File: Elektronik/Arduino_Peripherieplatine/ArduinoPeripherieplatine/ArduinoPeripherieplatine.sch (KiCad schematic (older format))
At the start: 31 parts

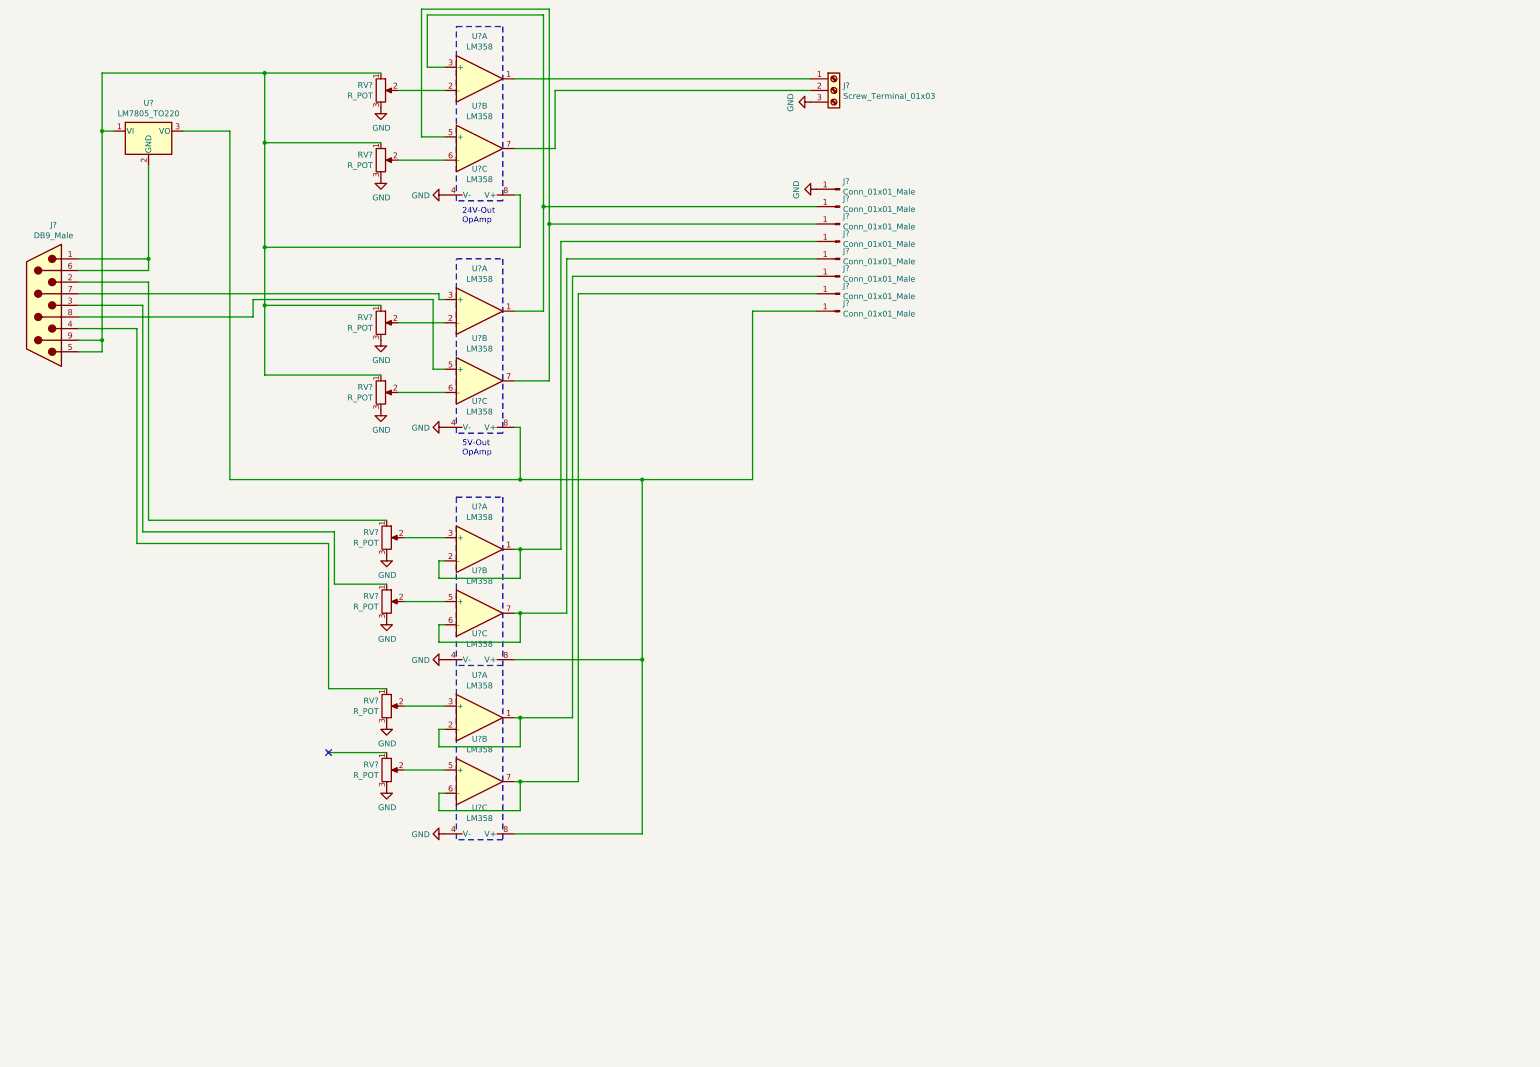
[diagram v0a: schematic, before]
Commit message: Updated Peripheral PCB
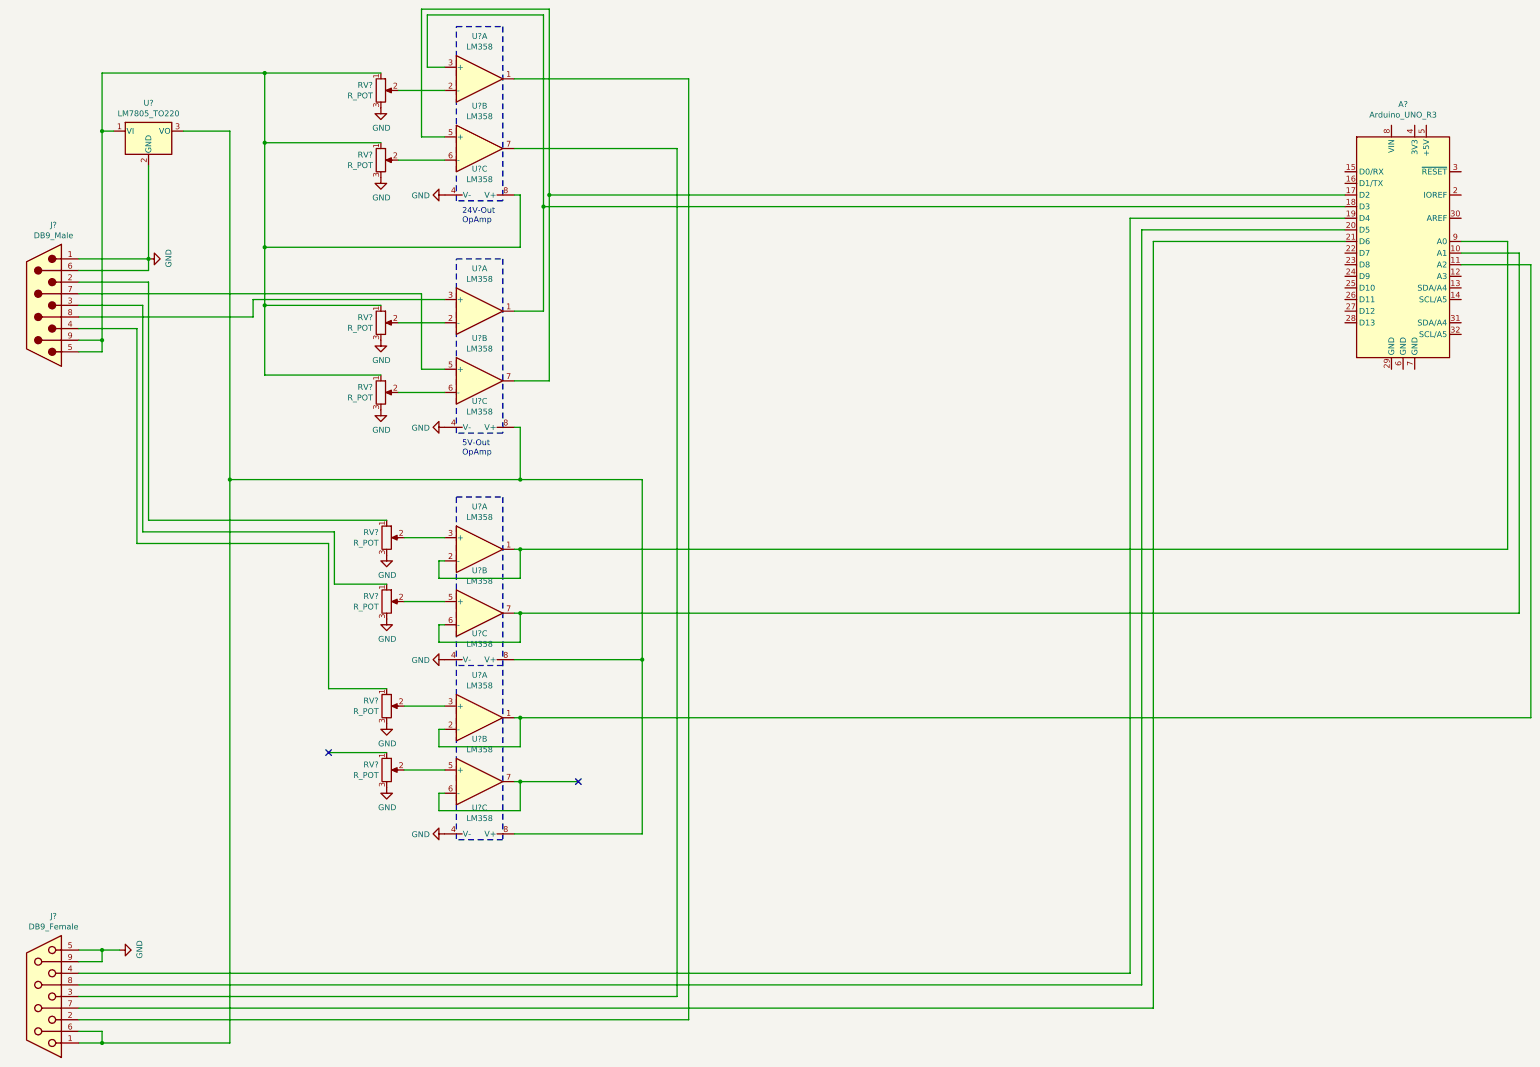
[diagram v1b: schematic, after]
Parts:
- removed J?: Screw_Terminal_01x03, symbol Connector:Screw_Terminal_01x03
- removed J? (x8): Conn_01x01_Male, symbol Connector:Conn_01x01_Male
- added A?: Arduino_UNO_R3, Module:Arduino_UNO_R3, symbol MCU_Module:Arduino_UNO_R3
- added J?: DB9_Female, symbol Connector:DB9_Female
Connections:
- net GND: now also J?.1, J?.6, U?.2 (GND), J?.5, J?.9
- net at U?.3 (VO), U?.8 (V+), U?.8 (V+)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: now also J?.1, J?.6
- net at U?.1: now also J?.2
- net at U?.1, U?.3 (+): now also A?.18 (D3)
- net at U?.5 (+), U?.7: now also A?.17 (D2)
- net at U?.7: now also J?.3
- net at U?.3 (+): now also J?.8; no longer J?.7
- net at U?.5 (+): now also J?.7; no longer J?.8
- net at U?.1, U?.2 (-): now also A?.9 (A0)
- net at U?.6 (-), U?.7: now also A?.10 (A1)
- net at U?.1, U?.2 (-): now also A?.11 (A2)
- new net: A?.19 (D4), J?.4
- new net: A?.21 (D6), J?.7
- new net: A?.20 (D5), J?.8
- no-connect marks 1 -> 2
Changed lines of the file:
@@
 EELAYER 30 0
 EELAYER END
-$Descr A4 11693 8268
+$Descr A3 16535 11693
 encoding utf-8
 Sheet 1 1
@@
 	4600 500  5700 500
 Wire Wire Line
-	5700 500  5700 2350
+	5700 500  5700 2100
 Wire Wire Line
 	5700 3700 5400 3700
@@
 Text Notes 4950 2350 0    50   ~ 0
 24V-Out\nOpAmp
-$Comp
-L Connector:Screw_Terminal_01x03 J?
-U 1 1 63429B53
-P 8150 1200
-F 0 "J?" H 8230 1242 50  0000 L CNN
-F 1 "Screw_Terminal_01x03" H 8230 1151 50  0000 L CNN
-F 2 "" H 8150 1200 50  0001 C CNN
-F 3 "~" H 8150 1200 50  0001 C CNN
-	1    8150 1200
-	1    0    0    -1
-$EndComp
-Wire Wire Line
-	5400 1100 7950 1100
-Wire Wire Line
-	5400 1700 5750 1700
-Wire Wire Line
-	5750 1700 5750 1200
-Wire Wire Line
-	5750 1200 7950 1200
-$Comp
-L power:GND #PWR?
-U 1 1 6342D1B7
-P 7950 1300
-F 0 "#PWR?" H 7950 1050 50  0001 C CNN
-F 1 "GND" H 7955 1127 50  0000 C CNN
-F 2 "" H 7950 1300 50  0001 C CNN
-F 3 "" H 7950 1300 50  0001 C CNN
-	1    7950 1300
-	0    1    1    0
-$EndComp
-$Comp
-L Connector:Conn_01x01_Male J?
-U 1 1 634336AF
-P 8200 2050
-F 0 "J?" H 8172 1982 50  0000 R CNN
-F 1 "Conn_01x01_Male" H 8172 2073 50  0000 R CNN
-F 2 "" H 8200 2050 50  0001 C CNN
-F 3 "~" H 8200 2050 50  0001 C CNN
-	1    8200 2050
-	-1   0    0    1
-$EndComp
-$Comp
-L Connector:Conn_01x01_Male J?
-U 1 1 63434368
-P 8200 2200
-F 0 "J?" H 8172 2132 50  0000 R CNN
-F 1 "Conn_01x01_Male" H 8172 2223 50  0000 R CNN
-F 2 "" H 8200 2200 50  0001 C CNN
-F 3 "~" H 8200 2200 50  0001 C CNN
-	1    8200 2200
-	-1   0    0    1
-$EndComp
-$Comp
-L Connector:Conn_01x01_Male J?
-U 1 1 634347F4
-P 8200 2350
-F 0 "J?" H 8172 2282 50  0000 R CNN
-F 1 "Conn_01x01_Male" H 8172 2373 50  0000 R CNN
-F 2 "" H 8200 2350 50  0001 C CNN
-F 3 "~" H 8200 2350 50  0001 C CNN
-	1    8200 2350
-	-1   0    0    1
-$EndComp
-$Comp
-L Connector:Conn_01x01_Male J?
-U 1 1 63434E46
-P 8200 2500
-F 0 "J?" H 8172 2432 50  0000 R CNN
-F 1 "Conn_01x01_Male" H 8172 2523 50  0000 R CNN
-F 2 "" H 8200 2500 50  0001 C CNN
-F 3 "~" H 8200 2500 50  0001 C CNN
-	1    8200 2500
-	-1   0    0    1
-$EndComp
-$Comp
-L Connector:Conn_01x01_Male J?
-U 1 1 63435092
-P 8200 2650
-F 0 "J?" H 8172 2582 50  0000 R CNN
-F 1 "Conn_01x01_Male" H 8172 2673 50  0000 R CNN
-F 2 "" H 8200 2650 50  0001 C CNN
-F 3 "~" H 8200 2650 50  0001 C CNN
-	1    8200 2650
-	-1   0    0    1
-$EndComp
-$Comp
-L Connector:Conn_01x01_Male J?
-U 1 1 63435409
-P 8200 2800
-F 0 "J?" H 8172 2732 50  0000 R CNN
-F 1 "Conn_01x01_Male" H 8172 2823 50  0000 R CNN
-F 2 "" H 8200 2800 50  0001 C CNN
-F 3 "~" H 8200 2800 50  0001 C CNN
-	1    8200 2800
-	-1   0    0    1
-$EndComp
-$Comp
-L Connector:Conn_01x01_Male J?
-U 1 1 634355C3
-P 8200 2950
-F 0 "J?" H 8172 2882 50  0000 R CNN
-F 1 "Conn_01x01_Male" H 8172 2973 50  0000 R CNN
-F 2 "" H 8200 2950 50  0001 C CNN
-F 3 "~" H 8200 2950 50  0001 C CNN
-	1    8200 2950
-	-1   0    0    1
-$EndComp
-$Comp
-L Connector:Conn_01x01_Male J?
-U 1 1 63435818
-P 8200 3100
-F 0 "J?" H 8172 3032 50  0000 R CNN
-F 1 "Conn_01x01_Male" H 8172 3123 50  0000 R CNN
-F 2 "" H 8200 3100 50  0001 C CNN
-F 3 "~" H 8200 3100 50  0001 C CNN
-	1    8200 3100
-	-1   0    0    1
-$EndComp
+Wire Wire Line
+	5400 1100 6900 1100
 Wire Wire Line
 	5450 4550 6500 4550
-Wire Wire Line
-	7450 4550 7450 3100
-Wire Wire Line
-	7450 3100 8000 3100
 Connection ~ 5450 4550
-$Comp
-L power:GND #PWR?
-U 1 1 63436912
-P 8000 2050
-F 0 "#PWR?" H 8000 1800 50  0001 C CNN
-F 1 "GND" H 8005 1877 50  0000 C CNN
-F 2 "" H 8000 2050 50  0001 C CNN
-F 3 "" H 8000 2050 50  0001 C CNN
-	1    8000 2050
-	0    1    1    0
-$EndComp
-Wire Wire Line
-	8000 2200 5650 2200
 Connection ~ 5650 2200
 Wire Wire Line
 	5650 2200 5650 550
-Wire Wire Line
-	8000 2350 5700 2350
-Connection ~ 5700 2350
-Wire Wire Line
-	5700 2350 5700 3700
 $Comp
 L Amplifier_Operational:LM358 U?
@@
 Wire Wire Line
 	6500 7600 6500 6100
-Connection ~ 6500 4550
-Wire Wire Line
-	6500 4550 7450 4550
 Wire Wire Line
 	5400 6100 6500 6100
@@
 Wire Wire Line
 	4750 7250 4800 7250
-Wire Wire Line
-	5450 5150 5800 5150
-Wire Wire Line
-	5800 5150 5800 2500
-Wire Wire Line
-	5800 2500 8000 2500
 Connection ~ 5450 5150
-Wire Wire Line
-	5450 5700 5850 5700
-Wire Wire Line
-	5850 5700 5850 2650
-Wire Wire Line
-	5850 2650 8000 2650
 Connection ~ 5450 5700
-Wire Wire Line
-	5450 6600 5900 6600
-Wire Wire Line
-	5900 6600 5900 2800
-Wire Wire Line
-	5900 2800 8000 2800
 Connection ~ 5450 6600
 Wire Wire Line
 	5450 7150 5950 7150
-Wire Wire Line
-	5950 7150 5950 2950
-Wire Wire Line
-	5950 2950 8000 2950
 Connection ~ 5450 7150
 $Comp
@@
 	1850 1050 3250 1050
 Wire Wire Line
-	1650 2950 4750 2950
-Wire Wire Line
-	4750 2950 4750 3000
-Wire Wire Line
-	4750 3000 4800 3000
-Wire Wire Line
 	1650 3150 3150 3150
 Wire Wire Line
 	3150 3150 3150 3000
-Wire Wire Line
-	3150 3000 4700 3000
-Wire Wire Line
-	4700 3000 4700 3600
-Wire Wire Line
-	4700 3600 4800 3600
 Wire Wire Line
 	1650 2850 2250 2850
@@
 Wire Wire Line
 	3800 6900 4300 6900
+$Comp
+L Connector:DB9_Female J?
+U 1 1 63636093
+P 1350 9000
+F 0 "J?" H 1268 8308 50  0000 C CNN
+F 1 "DB9_Female" H 1268 8399 50  0000 C CNN
+F 2 "" H 1350 9000 50  0001 C CNN
+F 3 " ~" H 1350 9000 50  0001 C CNN
+	1    1350 9000
+	-1   0    0    1
+$EndComp
+$Comp
+L power:GND #PWR?
+U 1 1 63639BB3
+P 2250 2650
+F 0 "#PWR?" H 2250 2400 50  0001 C CNN
+F 1 "GND" H 2255 2477 50  0000 C CNN
+F 2 "" H 2250 2650 50  0001 C CNN
+F 3 "" H 2250 2650 50  0001 C CNN
+	1    2250 2650
+	0    -1   -1   0
+$EndComp
+$Comp
+L MCU_Module:Arduino_UNO_R3 A?
+U 1 1 6363B884
+P 13050 2500
+F 0 "A?" H 13050 3681 50  0000 C CNN
+F 1 "Arduino_UNO_R3" H 13050 3590 50  0000 C CNN
+F 2 "Module:Arduino_UNO_R3" H 13050 2500 50  0001 C CIN
+F 3 "https://www.arduino.cc/en/Main/arduinoBoardUno" H 13050 2500 50  0001 C CNN
+	1    13050 2500
+	1    0    0    -1
+$EndComp
+Wire Wire Line
+	12550 2100 5700 2100
+Connection ~ 5700 2100
+Wire Wire Line
+	5650 2200 12550 2200
+Wire Wire Line
+	1650 8800 10700 8800
+Wire Wire Line
+	10700 8800 10700 2300
+Wire Wire Line
+	10700 2300 12550 2300
+Wire Wire Line
+	1650 8900 10800 8900
+Wire Wire Line
+	10800 8900 10800 2400
+Wire Wire Line
+	10800 2400 12550 2400
+Wire Wire Line
+	1650 9100 10900 9100
+Wire Wire Line
+	10900 9100 10900 2500
+Wire Wire Line
+	10900 2500 12550 2500
+Wire Wire Line
+	1650 9400 1850 9400
+Wire Wire Line
+	2950 9400 2950 4550
+Connection ~ 2950 4550
+Wire Wire Line
+	1650 9300 1850 9300
+Wire Wire Line
+	1850 9300 1850 9400
+Connection ~ 1850 9400
+Wire Wire Line
+	1850 9400 2950 9400
+Wire Wire Line
+	1650 8600 1850 8600
+Wire Wire Line
+	1650 8700 1850 8700
+Wire Wire Line
+	1850 8700 1850 8600
+Connection ~ 1850 8600
+Wire Wire Line
+	1850 8600 2000 8600
+$Comp
+L power:GND #PWR?
+U 1 1 63671D1E
+P 2000 8600
+F 0 "#PWR?" H 2000 8350 50  0001 C CNN
+F 1 "GND" H 2005 8427 50  0000 C CNN
+F 2 "" H 2000 8600 50  0001 C CNN
+F 3 "" H 2000 8600 50  0001 C CNN
+	1    2000 8600
+	0    -1   -1   0
+$EndComp
+Wire Wire Line
+	1650 9200 6900 9200
+Wire Wire Line
+	6900 9200 6900 1100
+Wire Wire Line
+	1650 9000 6800 9000
+Wire Wire Line
+	6800 9000 6800 1700
+Wire Wire Line
+	5400 1700 6800 1700
+Wire Wire Line
+	5700 2100 5700 3700
+NoConn ~ 5950 7150
+Wire Wire Line
+	3150 3000 4800 3000
+Wire Wire Line
+	4600 3600 4600 2950
+Wire Wire Line
+	4600 2950 1650 2950
+Wire Wire Line
+	4600 3600 4800 3600
+Wire Wire Line
+	13950 5150 13950 2500
+Wire Wire Line
+	13950 2500 13550 2500
+Wire Wire Line
+	5450 5150 13950 5150
+Wire Wire Line
+	14050 5700 14050 2600
+Wire Wire Line
+	14050 2600 13550 2600
+Wire Wire Line
+	5450 5700 14050 5700
+Wire Wire Line
+	14150 6600 14150 2700
+Wire Wire Line
+	14150 2700 13550 2700
+Wire Wire Line
+	5450 6600 14150 6600
 $EndSCHEMATC

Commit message: Refactoring & Documentation
-Refactored the Ardunio's Code controlling the cable-speed as well as the RPM-display
-Updated the documentation of the electronic's box
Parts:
- added RV?: R_POT, symbol Device:R_POT
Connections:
- net GND: now also RV?.3
- net at J?.1, J?.6, U?.3 (VO)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: now also A?.5 (+5V), J?.7
- net at U?.5 (+): now also RV?.2; no longer J?.7
- net at RV?.1: no longer J?.4
- new net: J?.4, RV?.1
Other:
- note added: "Shunt-Widerstand Strommodulation\nDrehratensensor Kardanwelle"
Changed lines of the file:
@@
 	2550 1550 2950 1550
 Wire Wire Line
-	2950 1550 2950 4550
+	2950 1550 2950 2950
 Wire Wire Line
 	3250 1050 3250 1650
@@
 	3850 5450 4300 5450
 Wire Wire Line
-	3800 5100 3800 6350
-Wire Wire Line
 	3800 6350 4300 6350
 $Comp
@@
 Wire Wire Line
 	1650 3250 2150 3250
-Wire Wire Line
-	2150 3250 2150 5100
-Wire Wire Line
-	2150 5100 3800 5100
 NoConn ~ 3800 6900
 Wire Wire Line
@@
 	3150 3000 4800 3000
 Wire Wire Line
-	4600 3600 4600 2950
-Wire Wire Line
-	4600 2950 1650 2950
-Wire Wire Line
-	4600 3600 4800 3600
-Wire Wire Line
 	13950 5150 13950 2500
 Wire Wire Line
@@
 Wire Wire Line
 	5450 6600 14150 6600
+Wire Wire Line
+	13250 1500 13250 1450
+Wire Wire Line
+	13250 1450 13400 1450
+Wire Wire Line
+	13400 1450 13400 1050
+Wire Wire Line
+	13400 1050 9000 1050
+Wire Wire Line
+	9000 1050 9000 4550
+Wire Wire Line
+	9000 4550 6500 4550
+Connection ~ 6500 4550
+$Comp
+L Device:R_POT RV?
+U 1 1 6417FA5F
+P 2300 6150
+F 0 "RV?" H 2231 6196 50  0000 R CNN
+F 1 "R_POT" H 2231 6105 50  0000 R CNN
+F 2 "" H 2300 6150 50  0001 C CNN
+F 3 "~" H 2300 6150 50  0001 C CNN
+	1    2300 6150
+	0    -1   -1   0
+$EndComp
+Wire Wire Line
+	2300 3600 4800 3600
+Wire Wire Line
+	2300 3600 2300 6000
+Wire Wire Line
+	1650 2950 2950 2950
+Connection ~ 2950 2950
+Wire Wire Line
+	2950 2950 2950 4550
+$Comp
+L power:GND #PWR?
+U 1 1 6418E4E2
+P 2450 6150
+F 0 "#PWR?" H 2450 5900 50  0001 C CNN
+F 1 "GND" H 2455 5977 50  0000 C CNN
+F 2 "" H 2450 6150 50  0001 C CNN
+F 3 "" H 2450 6150 50  0001 C CNN
+	1    2450 6150
+	0    -1   -1   0
+$EndComp
+Wire Wire Line
+	2150 3250 2150 6150
+Text Notes 1800 6700 0    50   ~ 0
+Shunt-Widerstand Strommodulation\nDrehratensensor Kardanwelle
 $EndSCHEMATC

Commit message: Updated description of electronic's box
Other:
- note added: "Shunt-Widerstand Strommodulation\nDrehratensensor Kardanwelle\n->Auf geringen Spannungsabfall einzustellen,\num Unterspannung am Raddrehzahlsensor zur\nvermeiden"
- note removed: "Shunt-Widerstand Strommodulation\nDrehratensensor Kardanwelle"
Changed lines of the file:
@@
 	13400 1450 13400 1050
 Wire Wire Line
-	13400 1050 9000 1050
-Wire Wire Line
-	9000 1050 9000 4550
-Wire Wire Line
-	9000 4550 6500 4550
+	13400 1050 10550 1050
 Connection ~ 6500 4550
 $Comp
@@
 Wire Wire Line
 	2150 3250 2150 6150
-Text Notes 1800 6700 0    50   ~ 0
-Shunt-Widerstand Strommodulation\nDrehratensensor Kardanwelle
+Text Notes 1050 6900 0    50   ~ 0
+Shunt-Widerstand Strommodulation\nDrehratensensor Kardanwelle\n->Auf geringen Spannungsabfall einzustellen,\num Unterspannung am Raddrehzahlsensor zur\nvermeiden
+Wire Wire Line
+	10550 4550 10550 1050
+Wire Wire Line
+	6500 4550 10550 4550
 $EndSCHEMATC
